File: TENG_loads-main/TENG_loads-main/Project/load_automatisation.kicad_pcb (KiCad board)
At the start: 2 copper layers, 263.4 x 251.4 mm, 131 parts, among them IC1 OPA2145IDR, IC10 TBD62083AFG, IC11 74HC238D,653, IC2 TBD62083AFG, IC3 TBD62083AFG, IC4 74HC238D,653, IC5 74HC238D,653, IC6 TBD62083AFG, IC7 TBD62083AFG, IC8 TBD62083AFG, IC9 OPA145IDBVT, J1 PowerNeg, J12 PH-2X05SG, J13 1757242, J2 1757242, J3 1757242, J30 1757349, J4 PowerIn, K1 V23079A1001B301, K10 IMC03TS, K11 V23079A1001B301, K12 V23079A1001B301, K13 V23079A1001B301, K14 IMC03TS, K15 IMC03TS, K16 IMC03TS, K17 V23079A1001B301, K18 V23079A1001B301, K19 V23079A1001B301, K2 V23079A1001B301, K20 V23079A1001B301, K21 V23079A1001B301, K22 IMC03TS, K23 IMC03TS, K24 IMC03TS, K25 IMC03TS, K26 IMC03TS, K27 V23079A1001B301, K28 V23079A1001B301, K29 V23079A1001B301, K3 V23079A1001B301, K30 IMC03TS, K31 IMC03TS, K32 IMC03TS, K33 V23079A1001B301, K34 V23079A1001B301, K35 V23079A1001B301, K36 V23079A1001B301, K37 V23079A1001B301, K38 IMC03TS, K39 IMC03TS, K4 V23079A1001B301, K40 IMC03TS, K41 IMC03TS, K42 IMC03TS, K43 V23079A1001B301, K44 V23079A1001B301, K45 V23079A1001B301, K46 IMC03TS, K47 IMC03TS, K48 IMC03TS, K5 V23079A1001B301, K6 IMC03TS, K7 IMC03TS, K8 IMC03TS, K9 IMC03TS, U1 AMS1117-5.0, U2 INA128, U3 AMS1117-5.0

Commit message: 3D Model bug fixes
Now it displays correctly the 3D model
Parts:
- IC1: footprint SamacSys_Parts:SOIC127P600X175-8N -> Library:SOIC127P600X175-8N
- IC10, IC2, IC3, IC6, IC7, IC8: footprint SamacSys_Parts:SOIC127P1030X245-18N -> Library:SOIC127P1030X245-18N
- J13, J2, J3: footprint SamacSys_Parts:1757242 -> Library:1757242
- J30: footprint SamacSys_Parts:SHDRRA12W103P0X508_1X12_6296X1200X875P -> Library:SHDRRA12W103P0X508_1X12_6296X1200X875P
- K1, K11, K12, K13, K17, K18, K19, K2, K20, K21, K27, K28, K29, K3, K33, K34, K35, K36, K37, K4, K43, K44, K45, K5: value V23079A1001B301 -> V23079C1103B301; footprint SamacSys_Parts:V23079A1001B301 -> Library:V23079A1001B301
- K10, K14, K15, K16, K22, K23, K24, K25, K26, K30, K31, K32, K38, K39, K40, K41, K42, K46, K47, K48, K6, K7, K8, K9: footprint SamacSys_Parts:IMC03TS -> Library:IMC03TS

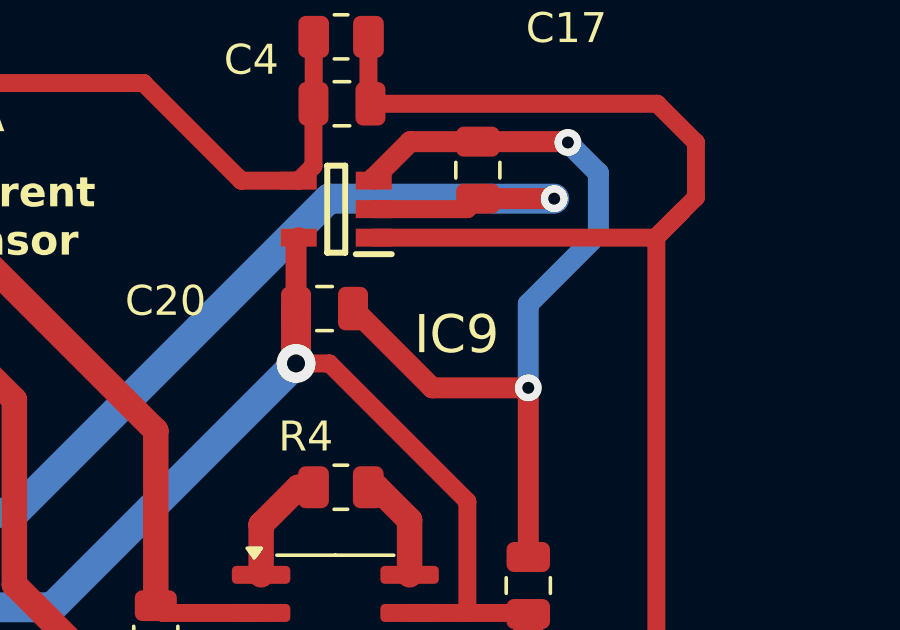
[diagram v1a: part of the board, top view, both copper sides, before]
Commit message: Solve 3D model bugs and add new models
Solve 3D model bugs and add new models.
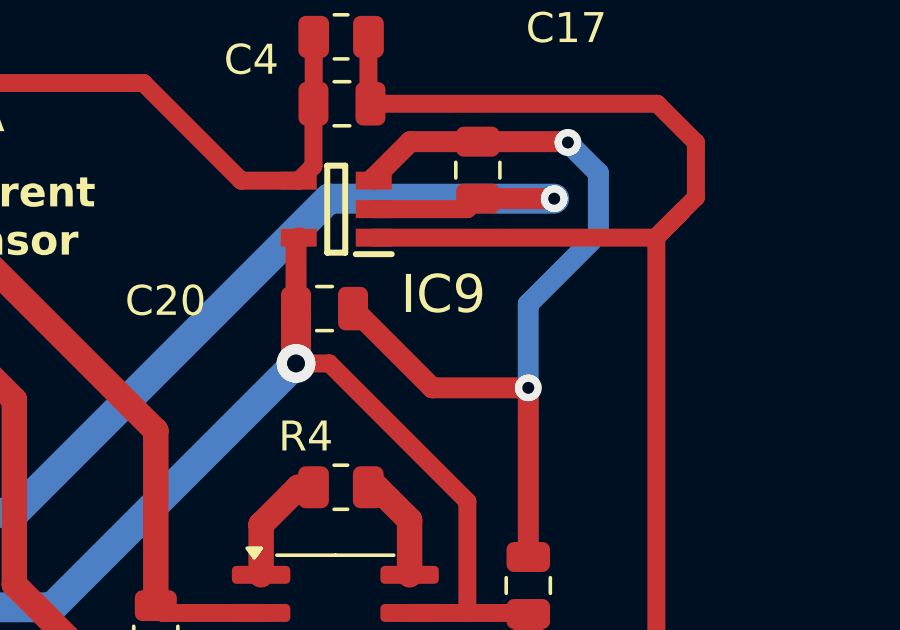
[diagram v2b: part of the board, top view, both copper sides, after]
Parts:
- IC9: footprint SamacSys_Parts:SOT95P280X145-5N -> Library:SOT95P280X145-5N
